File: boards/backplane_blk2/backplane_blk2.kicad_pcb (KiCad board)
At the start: 2 copper layers, 100.3 x 33 mm, 2 parts, among them J1 Conn_04x24, J2 DIN41612_03x32_C

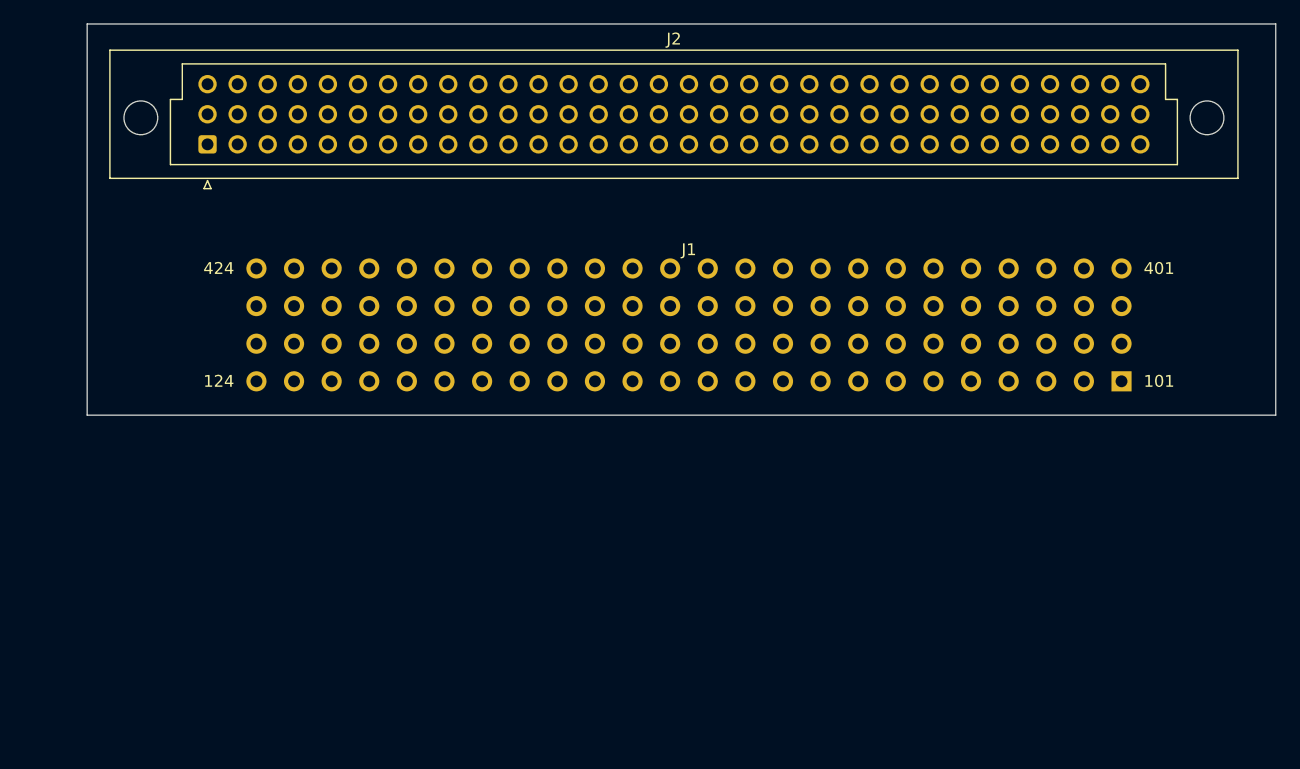
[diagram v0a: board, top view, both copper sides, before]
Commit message: Backplane-BLK2: Footprints laid out and preliminary sense routing
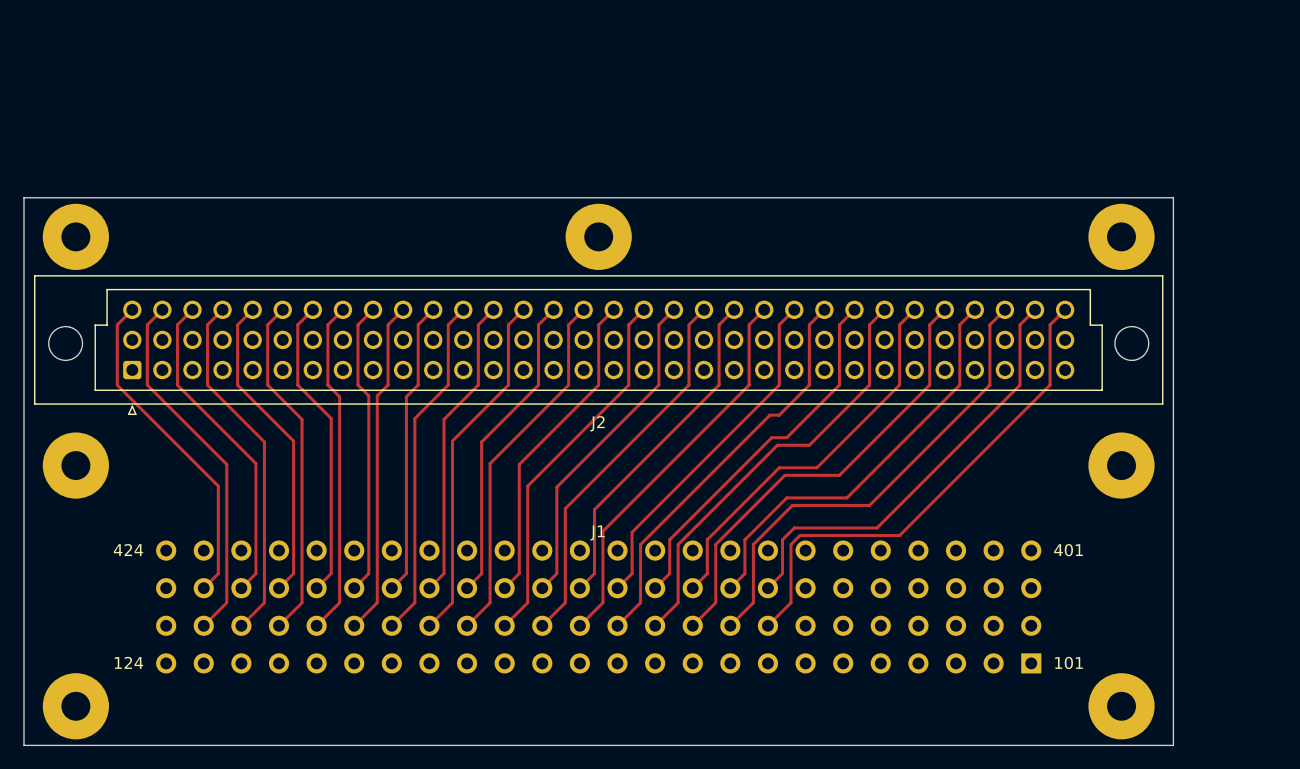
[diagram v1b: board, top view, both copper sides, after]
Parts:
- added H1: MountingHole_Pad, lachesis:MountingHole_No2_0.22in_Pad, F.Cu at (109.5, 117.3)
- added H2: MountingHole_Pad, lachesis:MountingHole_No2_0.22in_Pad, F.Cu at (109.5, 97.0)
- added H3: MountingHole_Pad, lachesis:MountingHole_No2_0.22in_Pad, F.Cu at (109.5, 77.7)
- added H4: MountingHole_Pad, lachesis:MountingHole_No2_0.22in_Pad, F.Cu at (153.7, 77.7)
- added H5: MountingHole_Pad, lachesis:MountingHole_No2_0.22in_Pad, F.Cu at (197.8, 77.7)
- added H6: MountingHole_Pad, lachesis:MountingHole_No2_0.22in_Pad, F.Cu at (197.8, 97.0)
- added H7: MountingHole_Pad, lachesis:MountingHole_No2_0.22in_Pad, F.Cu at (197.8, 117.3)
- moved J1 25.0 mm to (153.7, 108.9)
- moved J2 20.1 mm to (114.3, 88.9)
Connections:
- J1 pad 101: (no net) -> unconnected-(J1-Pad101)
- J1 pad 102: (no net) -> unconnected-(J1-Pad102)
- J1 pad 103: (no net) -> /SETARN
- J1 pad 104: (no net) -> /XSETAB
- J1 pad 105: (no net) -> /XPCN
- J1 pad 106: (no net) -> /XPFN
- J1 pad 107: (no net) -> /X01CN
- J1 pad 108: (no net) -> /X01FN
- J1 pad 109: (no net) -> /X02CN
- J1 pad 110: (no net) -> /X02FN
- J1 pad 111: (no net) -> /X03CN
- J1 pad 112: (no net) -> /X03FN
- J1 pad 113: (no net) -> /X04CN
- J1 pad 114: (no net) -> /X04FN
- J1 pad 115: (no net) -> /X05CN
- J1 pad 116: (no net) -> /X05FN
- J1 pad 117: (no net) -> /X06CN
- J1 pad 118: (no net) -> /X06FN
- J1 pad 119: (no net) -> /X07CN
- J1 pad 120: (no net) -> /X07FN
- J1 pad 121: (no net) -> /RSTRBD
- J1 pad 122: (no net) -> /XRSTBN
- J1 pad 123: (no net) -> /RSTRAD
- J1 pad 124: (no net) -> /XRSTAN
- J1 pad 201: (no net) -> /MODR1
- J1 pad 202: (no net) -> /STR11
- J1 pad 203: (no net) -> /STR09
- J1 pad 204: (no net) -> /STR07
- J1 pad 205: (no net) -> /STR05
- J1 pad 206: (no net) -> /STR03
- J1 pad 207: (no net) -> /STR01
- J1 pad 208: (no net) -> /GBR16
- J1 pad 209: (no net) -> /GBR14
- J1 pad 210: (no net) -> /GBR13
- J1 pad 211: (no net) -> /GBR12
- J1 pad 212: (no net) -> /GBR11
- J1 pad 213: (no net) -> /GBR10
- J1 pad 214: (no net) -> /GBR09
- J1 pad 215: (no net) -> /GBR08
- J1 pad 216: (no net) -> /GBR07
- J1 pad 217: (no net) -> /GBR06
- J1 pad 218: (no net) -> /GBR05
- J1 pad 219: (no net) -> /GBR04
- J1 pad 220: (no net) -> /GBR03
- J1 pad 221: (no net) -> /GBR02
- J1 pad 222: (no net) -> /GBR01
- J1 pad 223: (no net) -> /GBR15
- J1 pad 224: (no net) -> unconnected-(J1-Pad224)
- J1 pad 301: (no net) -> GND
- J1 pad 302: (no net) -> /STR02
- J1 pad 303: (no net) -> /STR04
- J1 pad 304: (no net) -> /STR06
- J1 pad 305: (no net) -> /STR08
- J1 pad 306: (no net) -> /STR10
- J1 pad 307: (no net) -> /STR12
- J1 pad 308: (no net) -> /GAR16
- J1 pad 309: (no net) -> /GAR14
- J1 pad 310: (no net) -> /GAR13
- J1 pad 311: (no net) -> /GAR12
- J1 pad 312: (no net) -> /GAR11
- J1 pad 313: (no net) -> /GAR10
- J1 pad 314: (no net) -> /GAR09
- J1 pad 315: (no net) -> /GAR08
- J1 pad 316: (no net) -> /GAR07
- J1 pad 317: (no net) -> /GAR06
- J1 pad 318: (no net) -> /GAR05
- J1 pad 319: (no net) -> /GAR04
- J1 pad 320: (no net) -> /GAR03
- J1 pad 321: (no net) -> /GAR02
- J1 pad 322: (no net) -> /GAR01
- J1 pad 323: (no net) -> /GAR15
- J1 pad 324: (no net) -> unconnected-(J1-Pad324)
- J1 pad 401: (no net) -> unconnected-(J1-Pad401)
- J1 pad 402: (no net) -> unconnected-(J1-Pad402)
- J1 pad 403: (no net) -> /XSETCD
- J1 pad 404: (no net) -> /SETCRN
- J1 pad 405: (no net) -> /RPCD
- J1 pad 406: (no net) -> /RPFD
- J1 pad 407: (no net) -> /R01CD
- J1 pad 408: (no net) -> /R01FD
- J1 pad 409: (no net) -> /R02CD
- J1 pad 410: (no net) -> /R02FD
- J1 pad 411: (no net) -> /R03CD
- J1 pad 412: (no net) -> /R03FD
- J1 pad 413: (no net) -> /R04CD
- J1 pad 414: (no net) -> /R04FD
- J1 pad 415: (no net) -> /R05CD
- J1 pad 416: (no net) -> /R05FD
- J1 pad 417: (no net) -> /R06CD
- J1 pad 418: (no net) -> /R06FD
- J1 pad 419: (no net) -> /R07CD
- J1 pad 420: (no net) -> /R07FD
- J1 pad 421: (no net) -> /XRSTDN
- J1 pad 422: (no net) -> /RSTRDD
- J1 pad 423: (no net) -> /XRSTCN
- J1 pad 424: (no net) -> /RSTRCD
- J2 pad a1: (no net) -> unconnected-(J2-Pada1)
- J2 pad a10: (no net) -> unconnected-(J2-Pada10)
- J2 pad a11: (no net) -> unconnected-(J2-Pada11)
- J2 pad a12: (no net) -> unconnected-(J2-Pada12)
- J2 pad a13: (no net) -> unconnected-(J2-Pada13)
- J2 pad a14: (no net) -> unconnected-(J2-Pada14)
- J2 pad a15: (no net) -> unconnected-(J2-Pada15)
- J2 pad a16: (no net) -> unconnected-(J2-Pada16)
- J2 pad a17: (no net) -> unconnected-(J2-Pada17)
- J2 pad a18: (no net) -> unconnected-(J2-Pada18)
- J2 pad a19: (no net) -> unconnected-(J2-Pada19)
- J2 pad a2: (no net) -> unconnected-(J2-Pada2)
- J2 pad a20: (no net) -> unconnected-(J2-Pada20)
- J2 pad a21: (no net) -> unconnected-(J2-Pada21)
- J2 pad a22: (no net) -> unconnected-(J2-Pada22)
- J2 pad a23: (no net) -> unconnected-(J2-Pada23)
- J2 pad a24: (no net) -> unconnected-(J2-Pada24)
- J2 pad a25: (no net) -> unconnected-(J2-Pada25)
- J2 pad a26: (no net) -> unconnected-(J2-Pada26)
- J2 pad a27: (no net) -> unconnected-(J2-Pada27)
- J2 pad a28: (no net) -> unconnected-(J2-Pada28)
- J2 pad a29: (no net) -> unconnected-(J2-Pada29)
- J2 pad a3: (no net) -> unconnected-(J2-Pada3)
- J2 pad a30: (no net) -> unconnected-(J2-Pada30)
- J2 pad a31: (no net) -> unconnected-(J2-Pada31)
- J2 pad a32: (no net) -> unconnected-(J2-Pada32)
- J2 pad a4: (no net) -> unconnected-(J2-Pada4)
- J2 pad a5: (no net) -> unconnected-(J2-Pada5)
- J2 pad a6: (no net) -> unconnected-(J2-Pada6)
- J2 pad a7: (no net) -> unconnected-(J2-Pada7)
- J2 pad a8: (no net) -> unconnected-(J2-Pada8)
- J2 pad a9: (no net) -> unconnected-(J2-Pada9)
- J2 pad b1: (no net) -> unconnected-(J2-Padb1)
- J2 pad b10: (no net) -> unconnected-(J2-Padb10)
- J2 pad b11: (no net) -> unconnected-(J2-Padb11)
- J2 pad b12: (no net) -> unconnected-(J2-Padb12)
- J2 pad b13: (no net) -> unconnected-(J2-Padb13)
- J2 pad b14: (no net) -> unconnected-(J2-Padb14)
- J2 pad b15: (no net) -> unconnected-(J2-Padb15)
- J2 pad b16: (no net) -> unconnected-(J2-Padb16)
- J2 pad b17: (no net) -> unconnected-(J2-Padb17)
- J2 pad b18: (no net) -> unconnected-(J2-Padb18)
- J2 pad b19: (no net) -> unconnected-(J2-Padb19)
- J2 pad b2: (no net) -> unconnected-(J2-Padb2)
- J2 pad b20: (no net) -> unconnected-(J2-Padb20)
- J2 pad b21: (no net) -> unconnected-(J2-Padb21)
- J2 pad b22: (no net) -> unconnected-(J2-Padb22)
- J2 pad b23: (no net) -> unconnected-(J2-Padb23)
- J2 pad b24: (no net) -> unconnected-(J2-Padb24)
- J2 pad b25: (no net) -> unconnected-(J2-Padb25)
- J2 pad b26: (no net) -> unconnected-(J2-Padb26)
- J2 pad b27: (no net) -> unconnected-(J2-Padb27)
- J2 pad b28: (no net) -> unconnected-(J2-Padb28)
- J2 pad b29: (no net) -> unconnected-(J2-Padb29)
- J2 pad b3: (no net) -> unconnected-(J2-Padb3)
- J2 pad b30: (no net) -> unconnected-(J2-Padb30)
- J2 pad b31: (no net) -> unconnected-(J2-Padb31)
- J2 pad b32: (no net) -> unconnected-(J2-Padb32)
- J2 pad b4: (no net) -> unconnected-(J2-Padb4)
- J2 pad b5: (no net) -> unconnected-(J2-Padb5)
- J2 pad b6: (no net) -> unconnected-(J2-Padb6)
- J2 pad b7: (no net) -> unconnected-(J2-Padb7)
- J2 pad b8: (no net) -> unconnected-(J2-Padb8)
- J2 pad b9: (no net) -> unconnected-(J2-Padb9)
- J2 pad c1: (no net) -> /GAR15
- J2 pad c10: (no net) -> /GBR04
- J2 pad c11: (no net) -> /GAR05
- J2 pad c12: (no net) -> /GBR05
- J2 pad c13: (no net) -> /GAR06
- J2 pad c14: (no net) -> /GBR06
- J2 pad c15: (no net) -> /GAR07
- J2 pad c16: (no net) -> /GBR07
- J2 pad c17: (no net) -> /GAR08
- J2 pad c18: (no net) -> /GBR08
- J2 pad c19: (no net) -> /GAR09
- J2 pad c2: (no net) -> /GBR15
- J2 pad c20: (no net) -> /GBR09
- J2 pad c21: (no net) -> /GAR10
- J2 pad c22: (no net) -> /GBR10
- J2 pad c23: (no net) -> /GAR11
- J2 pad c24: (no net) -> /GBR11
- J2 pad c25: (no net) -> /GAR12
- J2 pad c26: (no net) -> /GBR12
- J2 pad c27: (no net) -> /GAR13
- J2 pad c28: (no net) -> /GBR13
- J2 pad c29: (no net) -> /GAR14
- J2 pad c3: (no net) -> /GAR01
- J2 pad c30: (no net) -> /GBR14
- J2 pad c31: (no net) -> /GAR16
- J2 pad c32: (no net) -> /GBR16
- J2 pad c4: (no net) -> /GBR01
- J2 pad c5: (no net) -> /GAR02
- J2 pad c6: (no net) -> /GBR02
- J2 pad c7: (no net) -> /GAR03
- J2 pad c8: (no net) -> /GBR03
- J2 pad c9: (no net) -> /GAR04
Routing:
- net /GBR16: track 0.00 -> 42.0 mm
- net /GBR14: track 0.00 -> 40.1 mm
- net /GBR13: track 0.00 -> 38.2 mm
- net /GAR16: track 0.00 -> 36.9 mm
- net /GBR12: track 0.00 -> 36.3 mm
- net /GAR14: track 0.00 -> 35.0 mm
- net /GBR11: track 0.00 -> 34.4 mm
- net /GAR13: track 0.00 -> 33.1 mm
- net /GBR10: track 0.00 -> 33.1 mm
- net /GBR09: track 0.00 -> 32.3 mm
- net /GBR08: track 0.00 -> 31.5 mm
- net /GAR12: track 0.00 -> 31.2 mm
- net /GBR15: track 0.00 -> 30.8 mm
- net /GBR07: track 0.00 -> 30.7 mm
- net /GBR01: track 0.00 -> 30.0 mm
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- added copper zone on In1.Cu, net GND
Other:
- board size 100.3 x 33 mm -> 97 x 46.2 mm
- copper layers 2 -> 4
- net class Default removed

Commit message: Backplane: completed preliminary layout
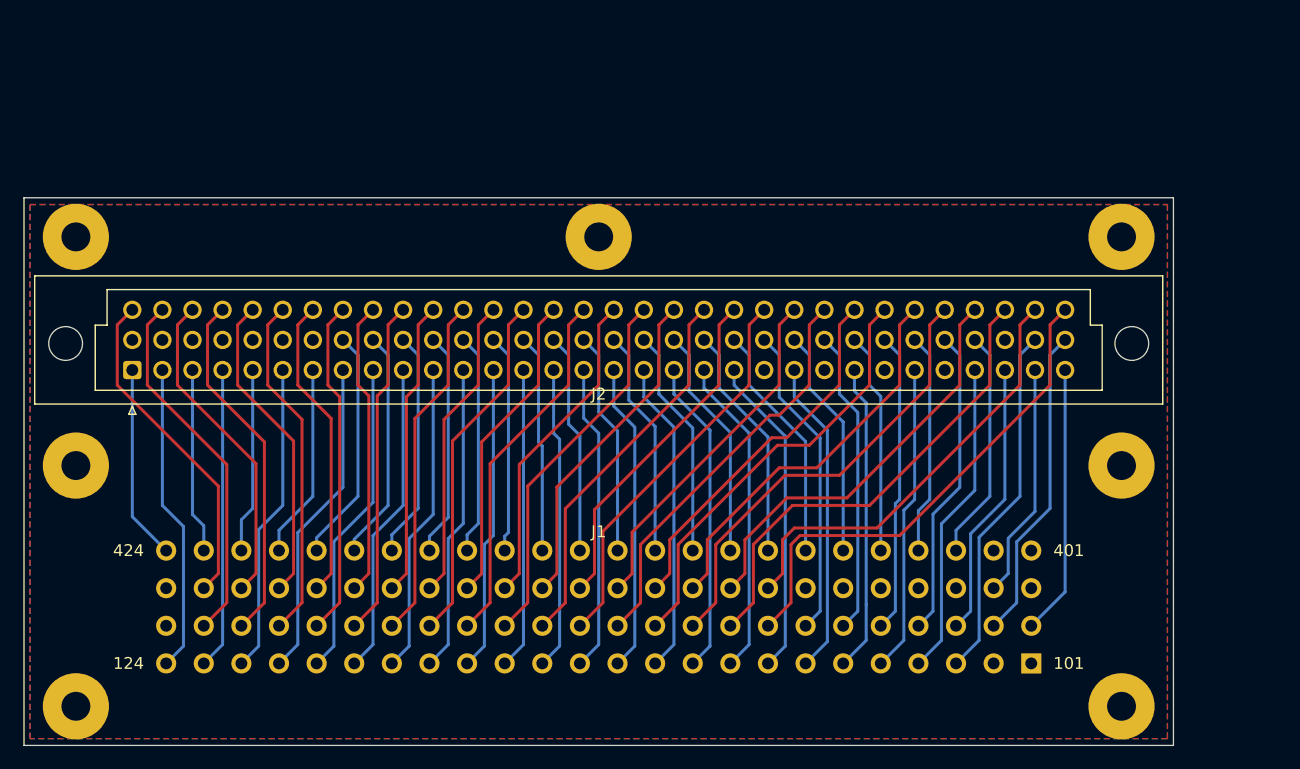
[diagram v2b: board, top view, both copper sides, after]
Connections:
- J2 pad a1: unconnected-(J2-Pada1) -> /RSTRCD
- J2 pad a10: unconnected-(J2-Pada10) -> /X07CN
- J2 pad a11: unconnected-(J2-Pada11) -> /X06FN
- J2 pad a12: unconnected-(J2-Pada12) -> /X06CN
- J2 pad a13: unconnected-(J2-Pada13) -> /X05FN
- J2 pad a14: unconnected-(J2-Pada14) -> /X05CN
- J2 pad a15: unconnected-(J2-Pada15) -> /X04FN
- J2 pad a16: unconnected-(J2-Pada16) -> /X04CN
- J2 pad a17: unconnected-(J2-Pada17) -> /X03FN
- J2 pad a18: unconnected-(J2-Pada18) -> /X03CN
- J2 pad a19: unconnected-(J2-Pada19) -> /X02FN
- J2 pad a2: unconnected-(J2-Pada2) -> /XRSTAN
- J2 pad a20: unconnected-(J2-Pada20) -> /X02CN
- J2 pad a21: unconnected-(J2-Pada21) -> /X01FN
- J2 pad a22: unconnected-(J2-Pada22) -> /STR12
- J2 pad a23: unconnected-(J2-Pada23) -> /X01CN
- J2 pad a24: unconnected-(J2-Pada24) -> /STR10
- J2 pad a25: unconnected-(J2-Pada25) -> /XPFN
- J2 pad a26: unconnected-(J2-Pada26) -> /STR08
- J2 pad a27: unconnected-(J2-Pada27) -> /XPCN
- J2 pad a28: unconnected-(J2-Pada28) -> /STR06
- J2 pad a29: unconnected-(J2-Pada29) -> /XSETAB
- J2 pad a3: unconnected-(J2-Pada3) -> /XRSTCN
- J2 pad a30: unconnected-(J2-Pada30) -> /STR09
- J2 pad a31: unconnected-(J2-Pada31) -> /STR02
- J2 pad a32: unconnected-(J2-Pada32) -> /MODR1
- J2 pad a4: unconnected-(J2-Pada4) -> /RSTRAD
- J2 pad a5: unconnected-(J2-Pada5) -> /RSTRDD
- J2 pad a6: unconnected-(J2-Pada6) -> /XRSTBN
- J2 pad a7: unconnected-(J2-Pada7) -> /XRSTDN
- J2 pad a8: unconnected-(J2-Pada8) -> /RSTRBD
- J2 pad a9: unconnected-(J2-Pada9) -> /X07FN
- J2 pad b1: unconnected-(J2-Padb1) -> GND
- J2 pad b10: unconnected-(J2-Padb10) -> /R06FD
- J2 pad b11: unconnected-(J2-Padb11) -> /R06CD
- J2 pad b12: unconnected-(J2-Padb12) -> /R05FD
- J2 pad b13: unconnected-(J2-Padb13) -> /R05CD
- J2 pad b14: unconnected-(J2-Padb14) -> /R04FD
- J2 pad b15: unconnected-(J2-Padb15) -> /R04CD
- J2 pad b16: unconnected-(J2-Padb16) -> /R03FD
- J2 pad b17: unconnected-(J2-Padb17) -> /R03CD
- J2 pad b18: unconnected-(J2-Padb18) -> /R02FD
- J2 pad b19: unconnected-(J2-Padb19) -> /R02CD
- J2 pad b2: unconnected-(J2-Padb2) -> GND
- J2 pad b20: unconnected-(J2-Padb20) -> /R01FD
- J2 pad b21: unconnected-(J2-Padb21) -> /R01CD
- J2 pad b22: unconnected-(J2-Padb22) -> /STR01
- J2 pad b23: unconnected-(J2-Padb23) -> /RPFD
- J2 pad b24: unconnected-(J2-Padb24) -> /STR03
- J2 pad b25: unconnected-(J2-Padb25) -> /RPCD
- J2 pad b26: unconnected-(J2-Padb26) -> /STR05
- J2 pad b27: unconnected-(J2-Padb27) -> /SETCRN
- J2 pad b28: unconnected-(J2-Padb28) -> /STR07
- J2 pad b29: unconnected-(J2-Padb29) -> /XSETCD
- J2 pad b3: unconnected-(J2-Padb3) -> GND
- J2 pad b30: unconnected-(J2-Padb30) -> /STR04
- J2 pad b31: unconnected-(J2-Padb31) -> /SETARN
- J2 pad b32: unconnected-(J2-Padb32) -> /STR11
- J2 pad b4: unconnected-(J2-Padb4) -> GND
- J2 pad b5: unconnected-(J2-Padb5) -> GND
- J2 pad b6: unconnected-(J2-Padb6) -> GND
- J2 pad b7: unconnected-(J2-Padb7) -> GND
- J2 pad b8: unconnected-(J2-Padb8) -> /R07FD
- J2 pad b9: unconnected-(J2-Padb9) -> /R07CD
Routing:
- net /SETARN: track 0.00 -> 30.1 mm
- net /X01FN: track 0.00 -> 27.2 mm
- net /X02CN: track 0.00 -> 27.0 mm
- net /RSTRBD: track 0.00 -> 27.0 mm
- net /X07FN: track 0.00 -> 26.7 mm
- net /XSETAB: track 0.00 -> 26.7 mm
- net /X01CN: track 0.00 -> 26.7 mm
- net /X02FN: track 0.00 -> 26.6 mm
- net /STR11: track 0.00 -> 26.6 mm
- net /STR01: track 0.00 -> 26.6 mm
- net /X03CN: track 0.00 -> 26.5 mm
- net /X07CN: track 0.00 -> 26.5 mm
- net /XRSTBN: track 0.00 -> 26.2 mm
- net /X06FN: track 0.00 -> 26.2 mm
- net /XRSTAN: track 0.00 -> 26.1 mm
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- added copper zone on B.Cu, net GND
- added copper zone on F.Cu, net GND
- added copper zone on In2.Cu, net GND
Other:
- board text added: "J2"

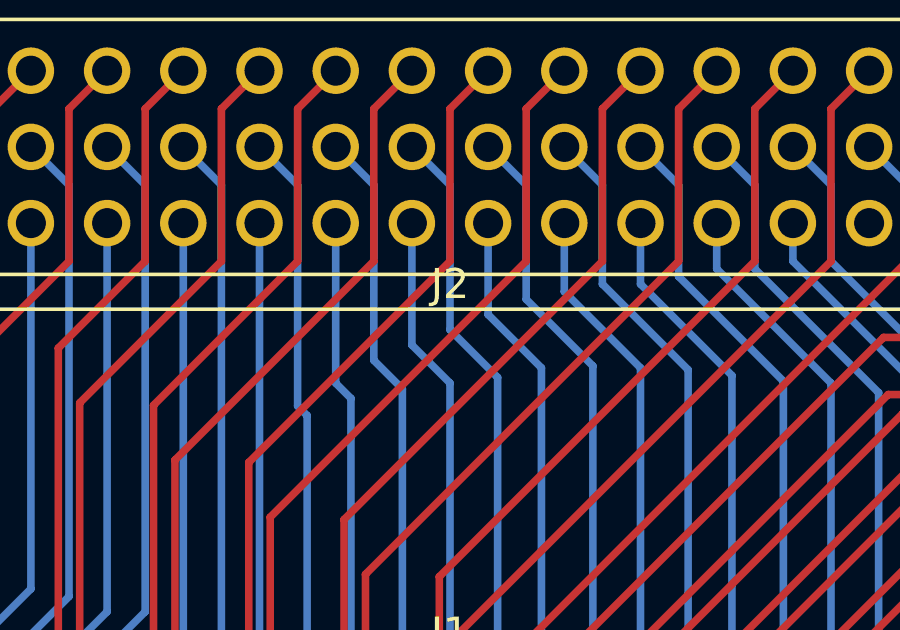
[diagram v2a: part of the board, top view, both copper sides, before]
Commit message: Backplane: a little bit of schematic and silkscreen cleanup
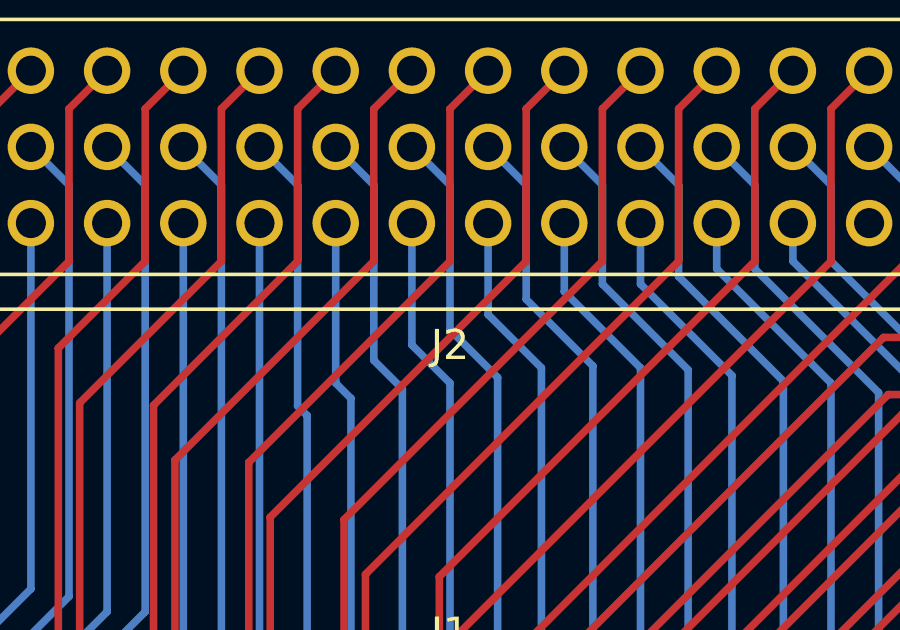
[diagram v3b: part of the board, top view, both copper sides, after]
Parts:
- added G***: LOGO, lachesis:backplane_cores, B.Cu at (153.7, 96.3)
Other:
- board text removed: "J2"

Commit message: Backplane: added a fancier rope graphic
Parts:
- removed the G*** at (153.7, 96.3)
- added G***: LOGO, lachesis:rope, B.Cu at (153.7, 96.5)
